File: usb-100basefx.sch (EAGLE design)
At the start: 57 parts, among them IC2 93LC66SN, U1 AX88772B, U2 AFBR-5803Z, U3 MICxxxx, Y1 25MHz

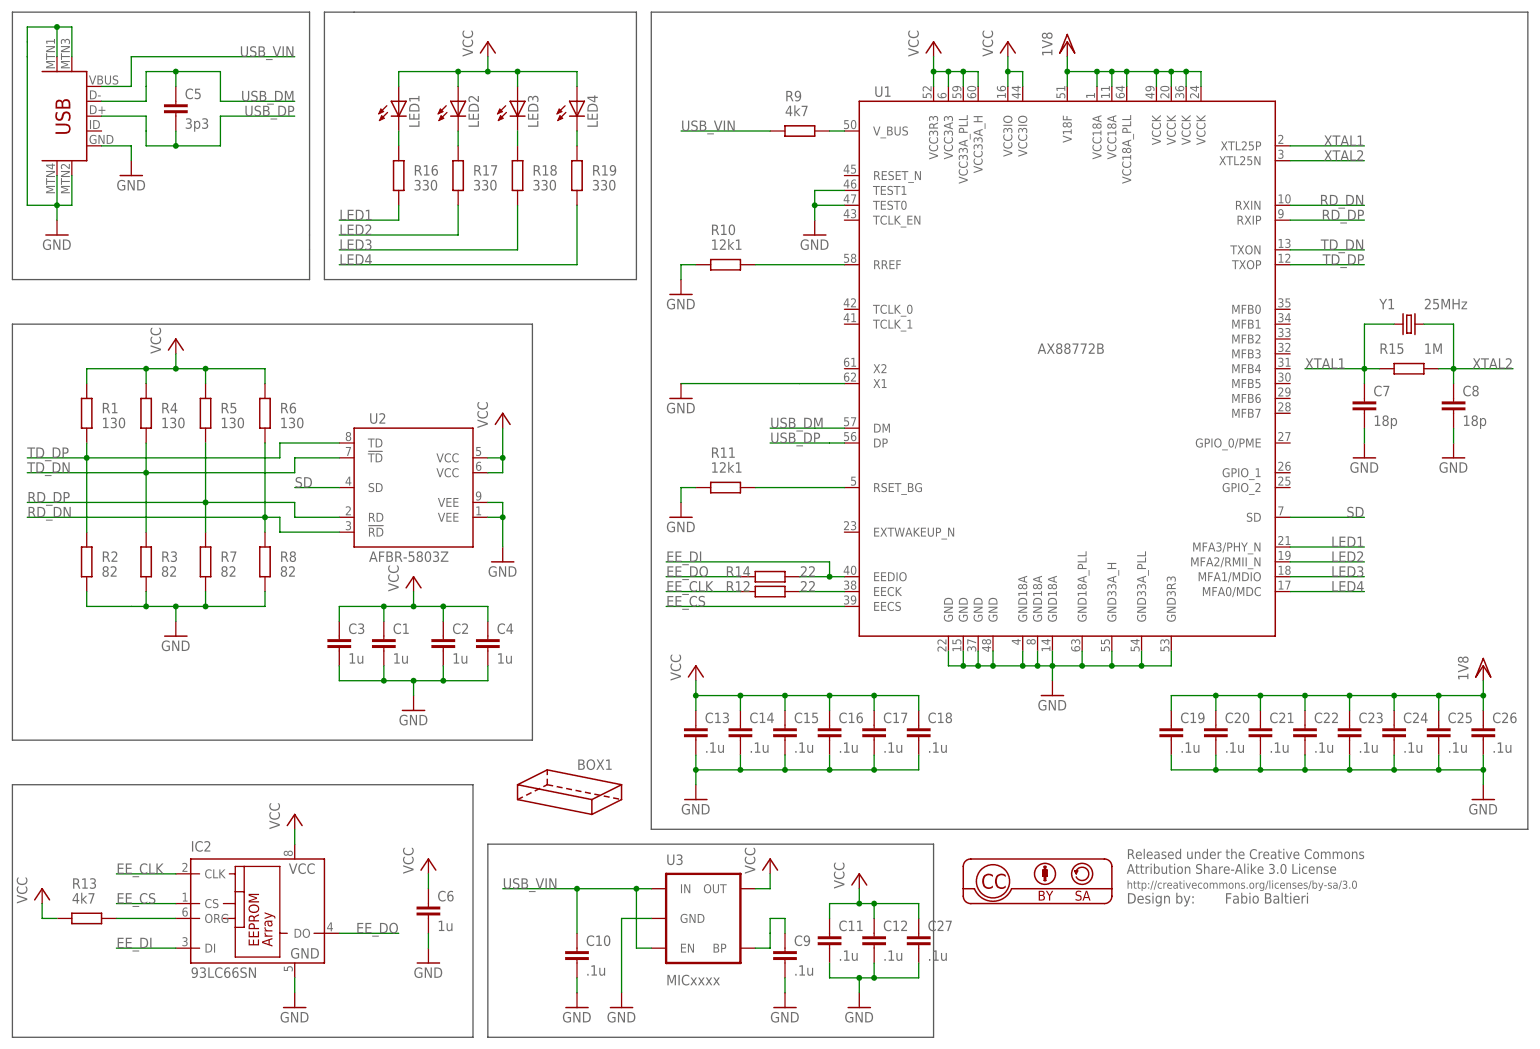
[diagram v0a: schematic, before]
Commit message: hw: use ld1117 for power
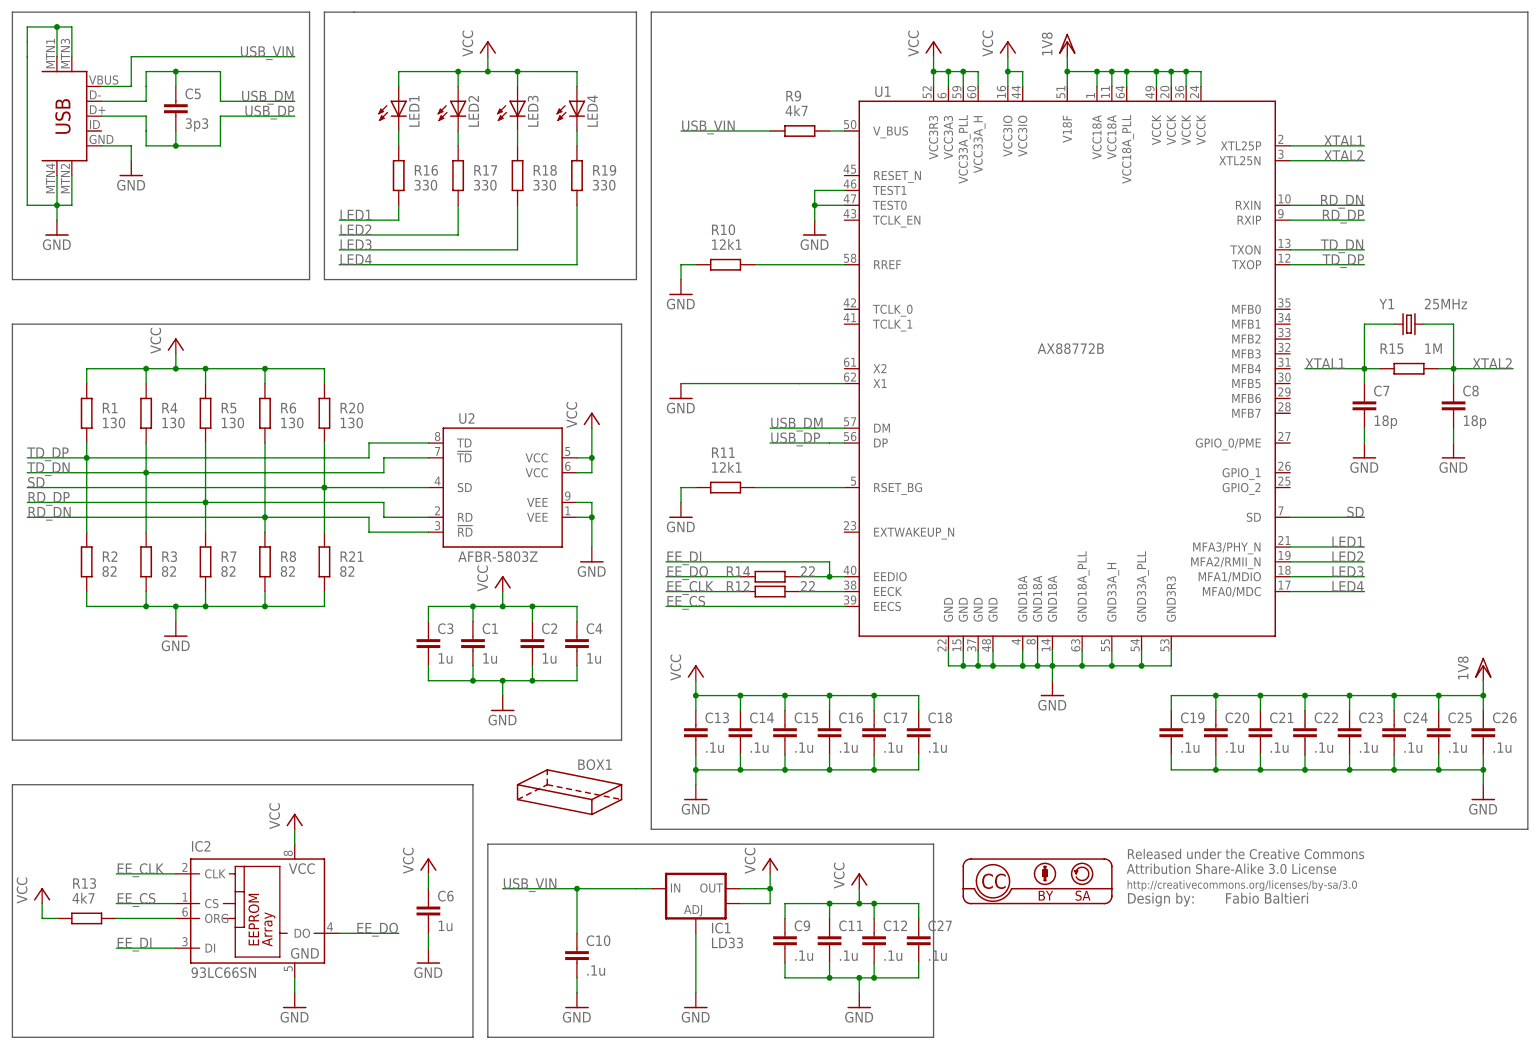
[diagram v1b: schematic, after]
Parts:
- removed U3: MICxxxx, SparkFun-PowerIC:V_REG_LDOSMD
- added IC1: LD33, SparkFun-PowerIC:V_REG_LM1117SOT223
- added R20: 130, rcl:R-EU_R0603
- added R21: 82, rcl:R-EU_R0603
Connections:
- removed net N$6: C9.1, U3.BP
- net GND: now also IC1.ADJ, R21.2; no longer U3.GND
- net SD: now also R20.2, R21.1
- net USB_VIN: now also IC1.IN; no longer U3.EN, U3.IN
- net VCC: now also C9.1, IC1.OUT, IC1.OUT@1, R20.1; no longer U3.OUT
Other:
- moved on the sheet: C1, C2, C3, C4, C9, U2
